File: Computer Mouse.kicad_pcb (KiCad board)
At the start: 2 copper layers, 117.3 x 74.1 mm, 86 parts, among them J1 Conn_01x05, J2 USB_C_Receptacle_USB2.0, J3 Conn_01x02, SW1 SW_SPST, SW2 SW_SPDT, SW3 SW_SPDT, SW4 RotaryEncoder, SW5 SW_SPDT, SW6 SW_SPDT, SW7 RotaryEncoder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

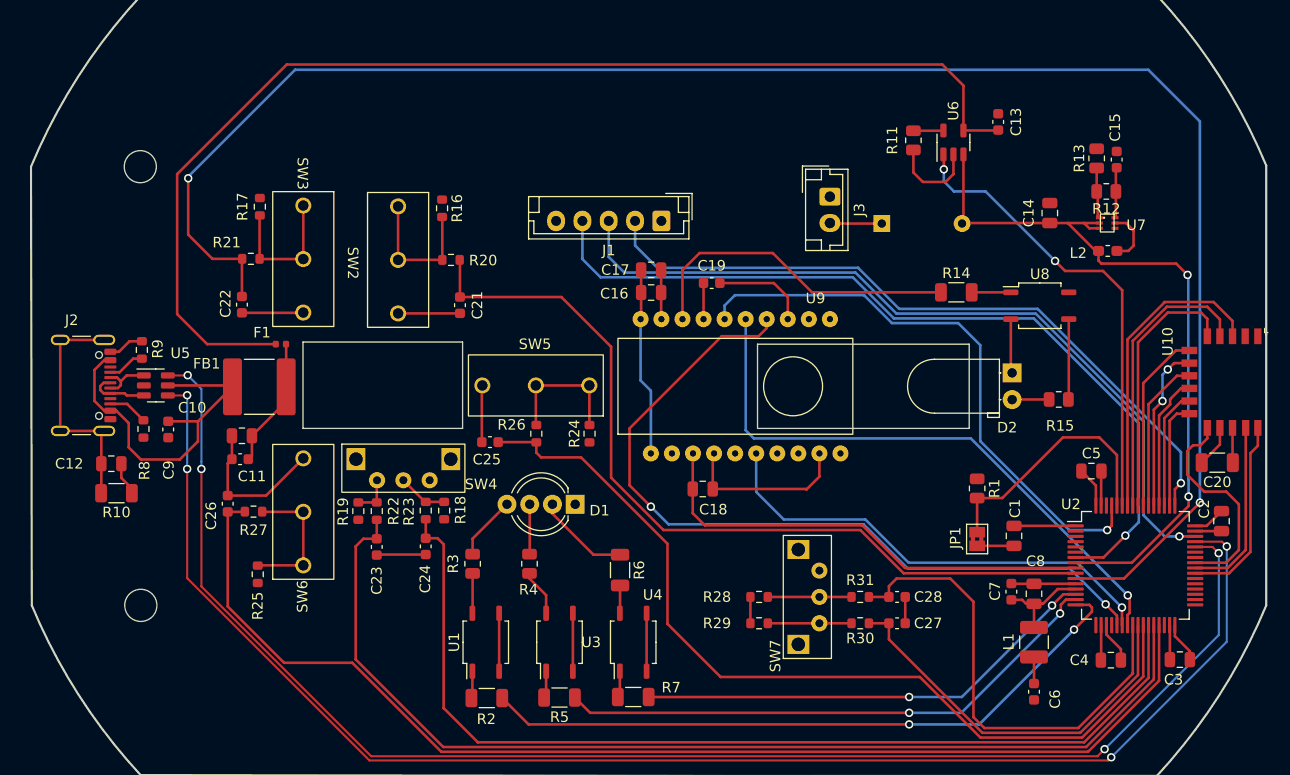
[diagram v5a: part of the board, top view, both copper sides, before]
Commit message: 3.3V paths, new usb module
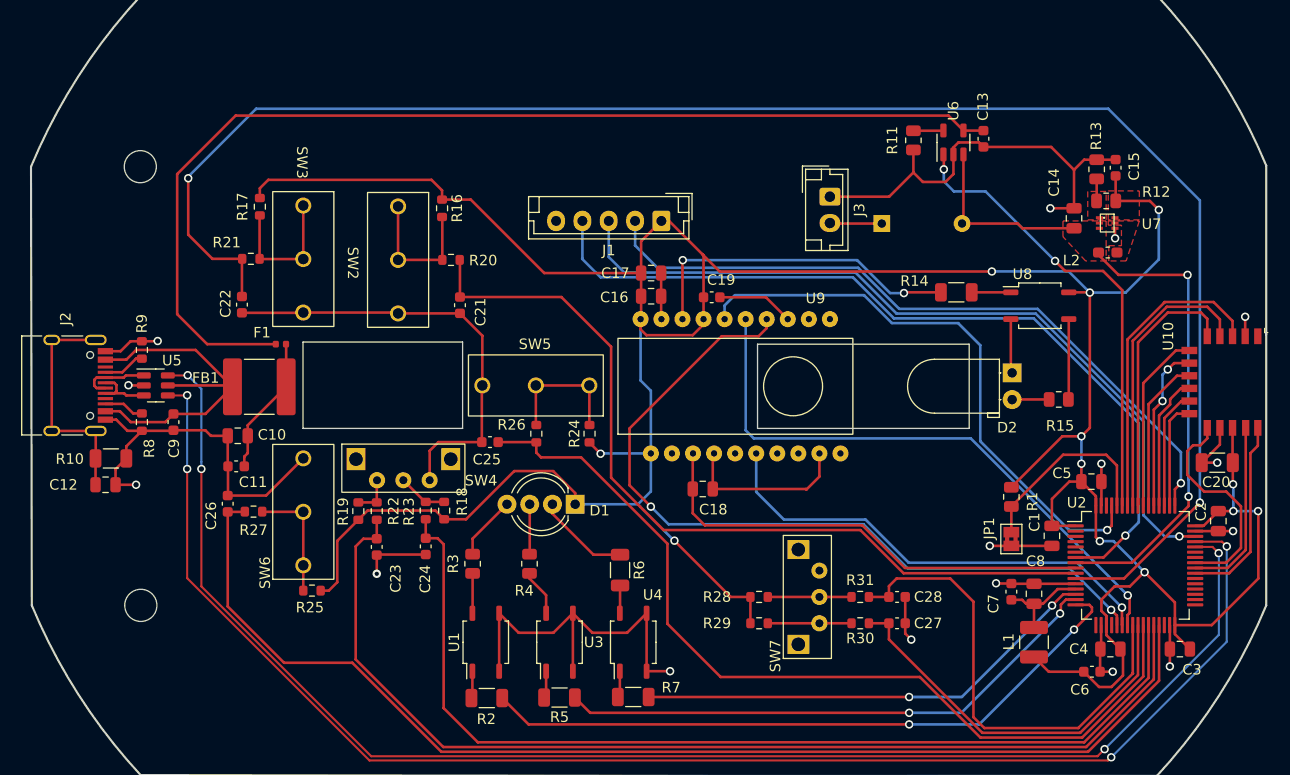
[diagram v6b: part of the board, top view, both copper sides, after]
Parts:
- J2: footprint Connector_USB:USB_C_Receptacle_GCT_USB4105-xx-A_16P_TopMnt_Horizontal -> Connector_USB:USB_C_Receptacle_HRO_TYPE-C-31-M-12
- moved C6 5.82 mm to (179.8, 128.1), turned to 0 degrees
- moved R25 5.38 mm to (105.8, 120.4), turned to 180 degrees
- moved C1 3.60 mm to (176.1, 115.2)
- moved R1 3.35 mm to (172.2, 111.5)
- moved R10 3.34 mm to (86.7, 107.8)
- moved JP1 3.25 mm to (172.2, 115.5)
- moved C14 2.35 mm to (178.2, 85.0)
- moved C13 2.13 mm to (169.6, 77.5), turned to -90 degrees
- moved C12 2.07 mm to (86.2, 110.3)
- moved C19 1.35 mm to (143.8, 92.5)
- moved C4 1.05 mm to (181.6, 126.0)
- moved R13 1.04 mm to (180.3, 80.4)
- moved C3 1.00 mm to (188.2, 126.0)
- moved C5 1.00 mm to (179.8, 110.0)
- moved R12 0.90 mm to (181.2, 83.4)
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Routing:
- net +3V3: track 55.4 -> 322.4 mm, vias 0 -> 12
- net GND: track 131.6 -> 242.6 mm, vias 0 -> 16
- net +BATT: track 70.9 -> 62.8 mm
- net +5V: track 111.2 -> 103.3 mm
- net SW3: track 168.4 -> 161.0 mm
- net Net-(JP1-A): track 24.4 -> 18.7 mm
- net Net-(U7-SW): track 5.28 -> 0.00 mm
- net Net-(C10-Pad2): track 12.4 -> 14.7 mm
- net Net-(U7-FB): track 4.04 -> 2.09 mm
- net Net-(SW6-A): track 13.3 -> 11.4 mm
- net Net-(J2-D--PadA7): track 5.04 -> 6.58 mm
- net Net-(J2-D+-PadA6): track 5.81 -> 6.58 mm
- net Net-(U5-VBUS): track 34.6 -> 34.0 mm
- net Net-(U9-XYLED): vias 0 -> 2
- added copper zone on F.Cu, net +3V3
- added copper zone on F.Cu, net +BATT
- added copper zone on F.Cu, net Net-(U7-FB)
- added copper zone on F.Cu, net Net-(U7-SW)

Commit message: GND fields
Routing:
- net GND: track 242.6 -> 151.5 mm, vias 16 -> 22
- net SW3: track 161.0 -> 161.6 mm, vias 2 -> 6
- net MOTION: track 55.1 -> 54.6 mm, vias 1 -> 5
- net MOSI: track 56.3 -> 56.6 mm, vias 1 -> 3
- added copper zone on B.Cu, net GND

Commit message: Readme update, gerber files
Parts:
- C1, C10, C2, C3, C4, C5, C8: value 100n -> 100nF
- C11, C6: value 4.7u -> 4.7uF
- C12: value 4.7n -> 4.7nF
- C20: value 10u -> 10uF
- C21, C22, C23, C24, C25, C26, C27, C28, C9: value 10n -> 10nF
- C7: value 1u -> 1uF
- F1: value 750m -> 750mA
- R10: value 1M -> 1MOhm
- R16, R17, R18, R19, R20, R21, R22, R23, R24, R25, R26, R27, R28, R29, R30, R31: value 1k -> 1kOhm
